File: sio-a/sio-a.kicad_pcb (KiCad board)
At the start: 2 copper layers, 99.1 x 99.1 mm, 37 parts, among them J1 DE9_Plug_MountingHoles, J2 Conn_01x06, J4 Conn_02x06_Odd_Even, J5 Conn_02x06_Odd_Even, J6 Conn_02x08_Odd_Even, J7 Conn_02x08_Odd_Even, J8 Conn_02x08_Odd_Even, Q1 BC547, U1 MAX232, U3 W65C22NxP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

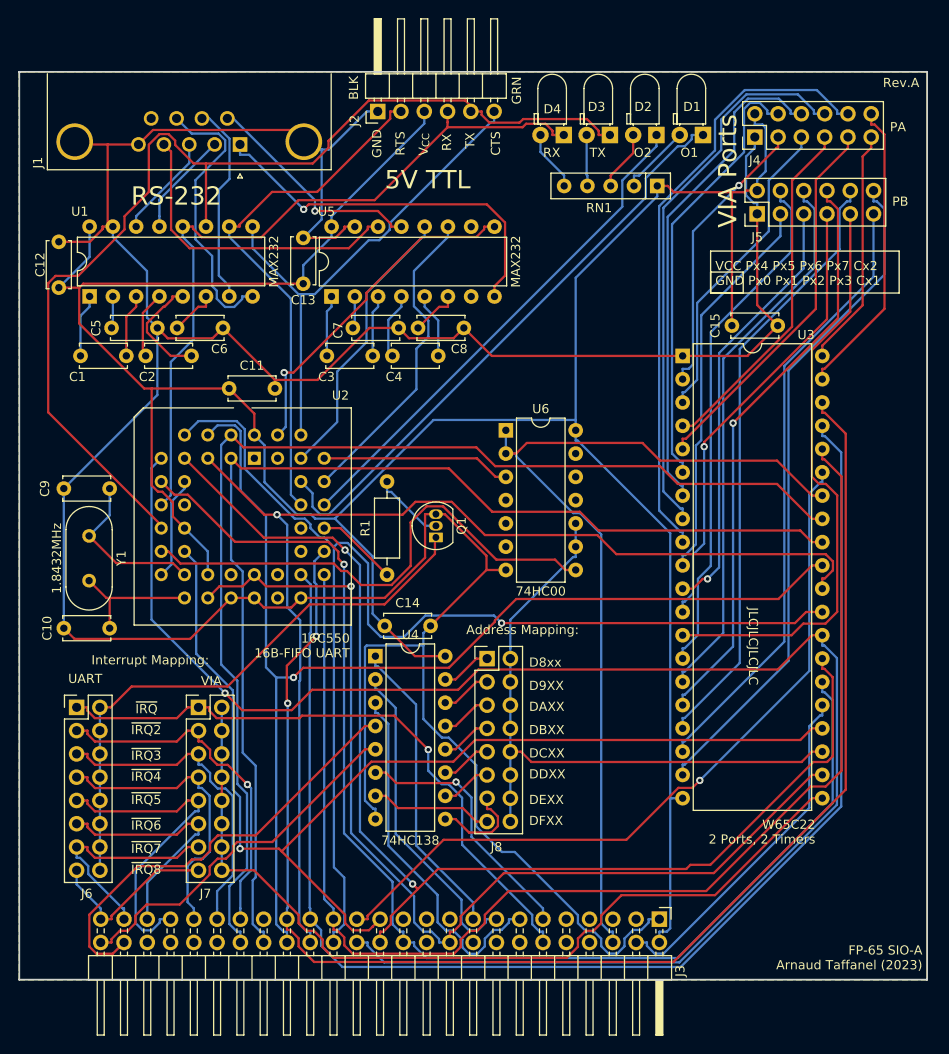
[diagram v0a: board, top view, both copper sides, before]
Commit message: Fix SIO-A CPU bus R/W logic
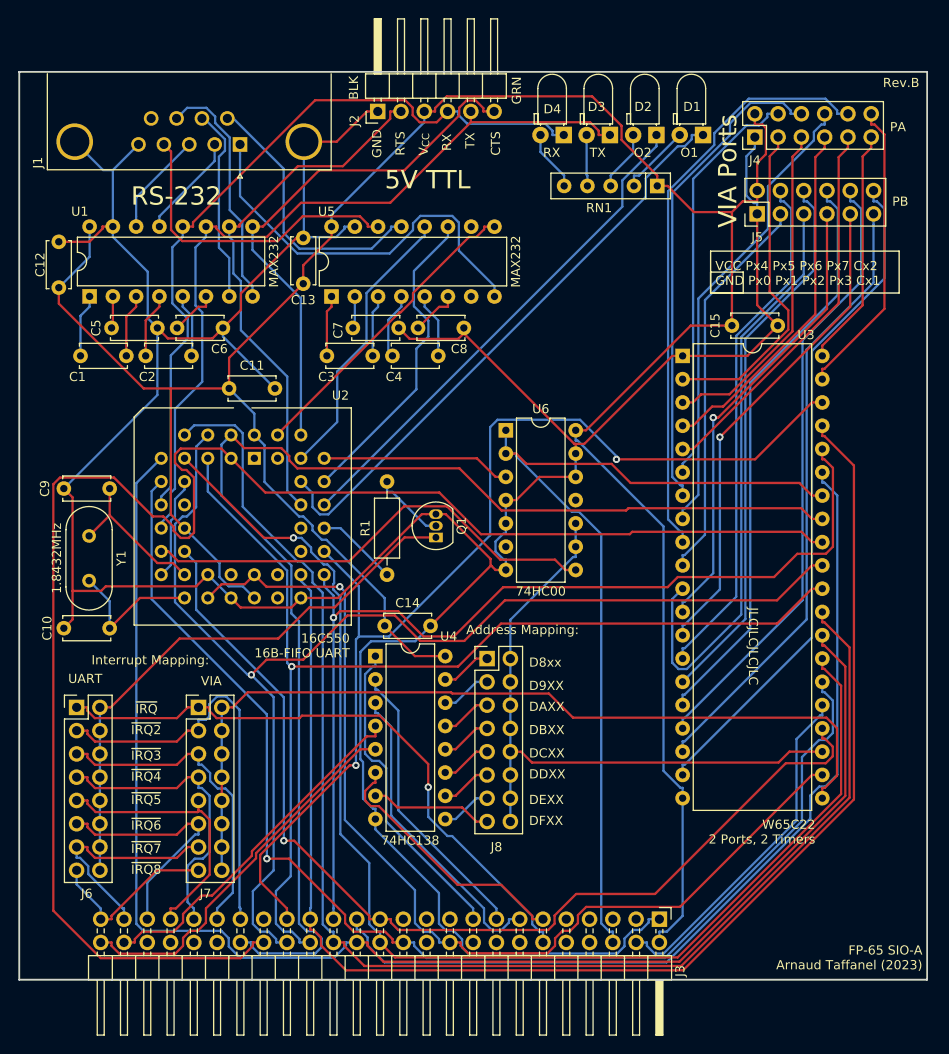
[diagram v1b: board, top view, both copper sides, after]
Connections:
- U2 pad 21: VCC -> GND
- U2 pad 24: GND -> VCC
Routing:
- net /D1: track 123.1 -> 176.5 mm
- net /A0: track 157.4 -> 119.6 mm
- net /A2: track 141.6 -> 109.3 mm, vias 0 -> 1
- net /TX: track 118.5 -> 87.4 mm
- net /D4: track 133.1 -> 154.1 mm, vias 1 -> 0
- net /D5: track 178.6 -> 159.5 mm, vias 1 -> 0
- net /PB1: track 47.3 -> 65.4 mm, vias 1 -> 0
- net /A3: track 83.2 -> 99.3 mm, vias 1 -> 0
- net VCC: track 307.8 -> 292.4 mm
- net /D0: track 126.8 -> 140.0 mm
- net /PB3: track 64.7 -> 53.7 mm, vias 0 -> 1
- net /PA6: track 60.7 -> 51.0 mm
- net /~{IO_SEL}: track 48.3 -> 38.9 mm
- net /D2: track 127.1 -> 135.1 mm
- net /A4: track 119.5 -> 112.5 mm
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- removed copper zone on B.Cu, net GND
- removed copper zone on F.Cu, net GND
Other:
- board text added: "Rev.B"
- board text removed: "Rev.A"

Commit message: Fix DB footprint on SCSI-A and SIO-A
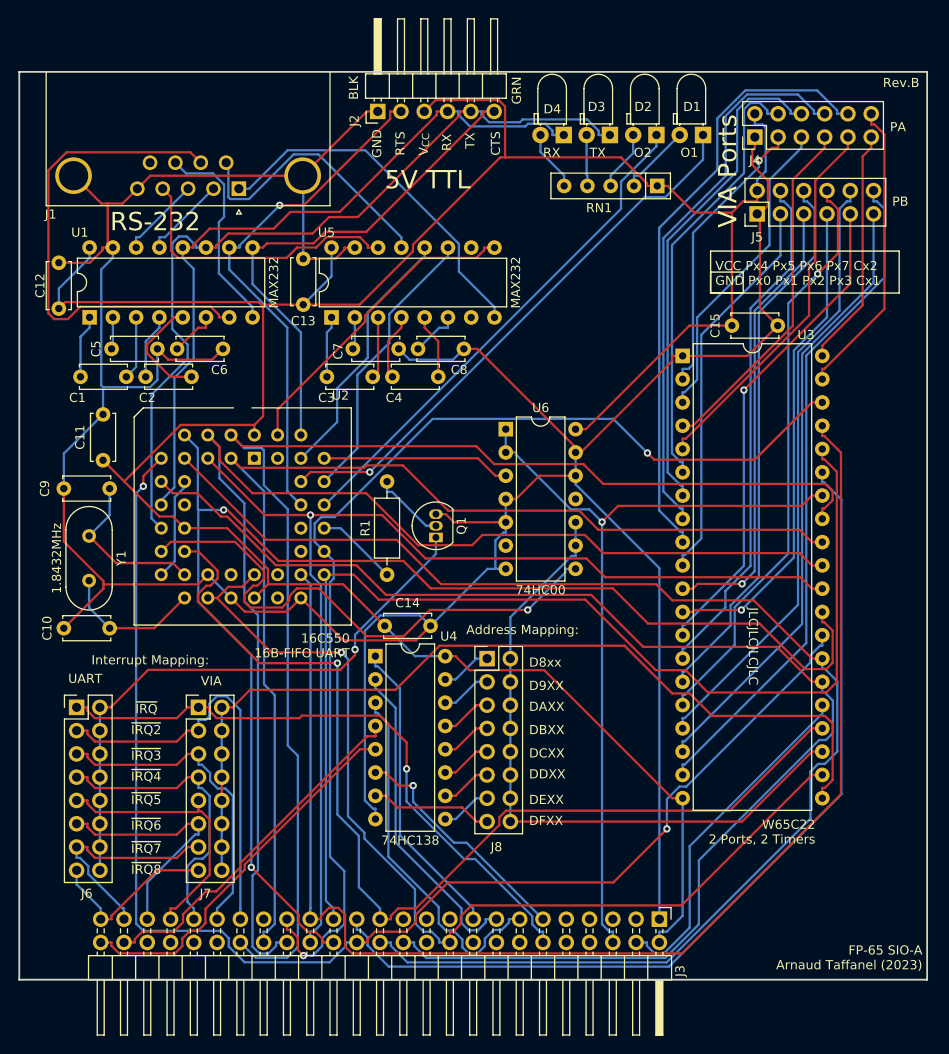
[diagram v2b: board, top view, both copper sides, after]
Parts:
- J1: footprint Connector_Dsub:DSUB-9_Male_Horizontal_P2.77x2.84mm_EdgePinOffset4.94mm_Housed_MountingHolesOffset7.48mm -> Connector_Dsub:DSUB-9_Male_Horizontal_P2.77x2.84mm_EdgePinOffset9.90mm_Housed_MountingHolesOffset11.32mm
- moved C11 15.8 mm to (108.7, 101.1), turned to 90 degrees
- moved J1 4.83 mm to (123.5, 71.4)
- moved C12 2.29 mm to (103.9, 84.5)
- moved C13 2.29 mm to (130.6, 84.1)
- moved C5 2.29 mm to (109.6, 88.9)
- moved C6 2.29 mm to (116.8, 88.9)
- moved C7 2.29 mm to (141.0, 88.9)
- moved C8 2.29 mm to (143.1, 88.9)
- moved U1 2.29 mm to (107.2, 85.5)
- moved U5 2.29 mm to (133.6, 85.5)
- moved C1 2.29 mm to (106.3, 91.9)
- moved C2 2.29 mm to (113.4, 91.9)
- moved C3 2.29 mm to (133.1, 91.9)
- moved C4 2.29 mm to (140.3, 91.9)
- moved U6 0.12 mm to (152.7, 97.7)
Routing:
- net /D1: track 176.5 -> 124.0 mm
- net /RTS: track 21.3 -> 54.7 mm
- net /A2: track 109.3 -> 126.0 mm, vias 1 -> 0
- net /PB1: track 65.4 -> 49.9 mm, vias 0 -> 1
- net /D7: track 134.5 -> 149.4 mm, vias 1 -> 0
- net /D6: track 138.7 -> 153.2 mm, vias 1 -> 0
- net /D5: track 159.5 -> 147.8 mm, vias 0 -> 2
- net /~{RES}: track 98.5 -> 88.1 mm, vias 0 -> 1
- net /PA6: track 51.0 -> 60.6 mm
- net /CS: track 51.0 -> 60.4 mm, vias 0 -> 1
- net /D4: track 154.1 -> 146.2 mm, vias 0 -> 2
- net /A10: track 34.0 -> 40.0 mm
- net Net-(U1-C2-): track 6.94 -> 12.0 mm
- net GND: track 363.3 -> 368.2 mm
- net /CD: track 44.2 -> 39.6 mm
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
